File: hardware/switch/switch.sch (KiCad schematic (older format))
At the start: 27 parts, among them J1 Conn_01x07, J2 Conn_01x03, J3 Conn_01x05, J4 Conn_01x04, K1 G6SU-2, K2 G6SU-2, K3 G6SU-2, K4 G6SU-2, SW1 D2F-01, SW2 D2F-01, SW3 D2F-01, SW4 D2F-01, U1 NCV7718CDQR2G, U2 STM32F042F6Px, U3 NCV7428MW3

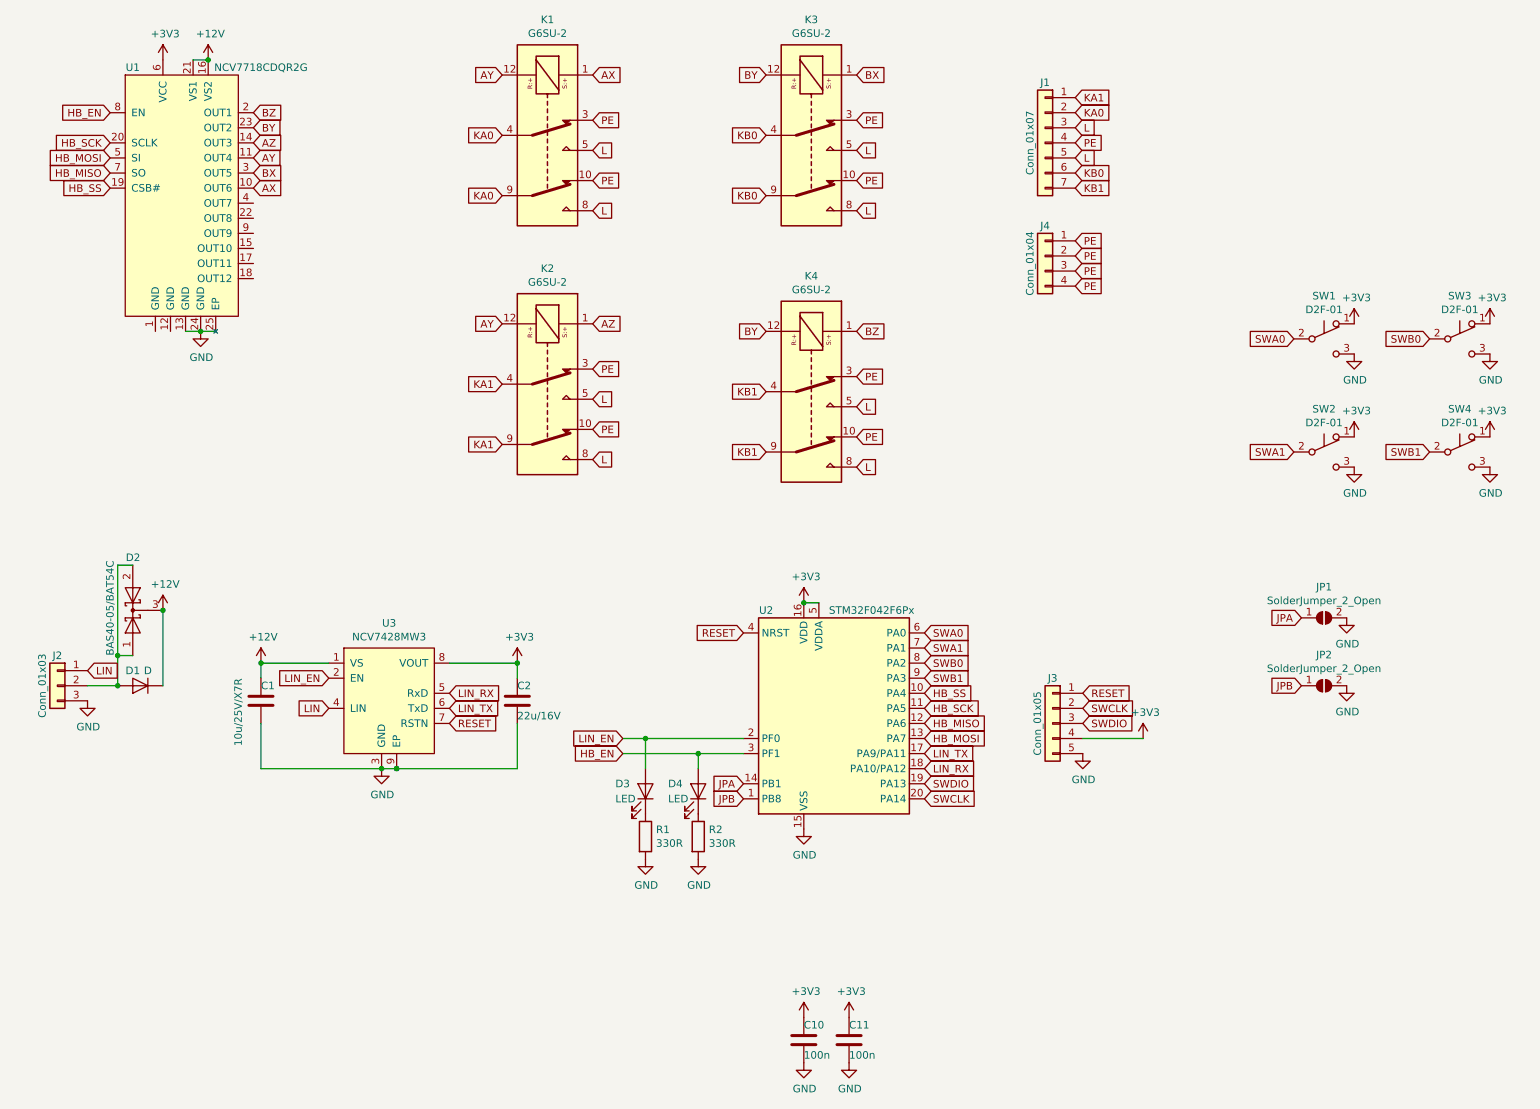
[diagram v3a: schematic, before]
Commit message: Add indicator LEDs to switch
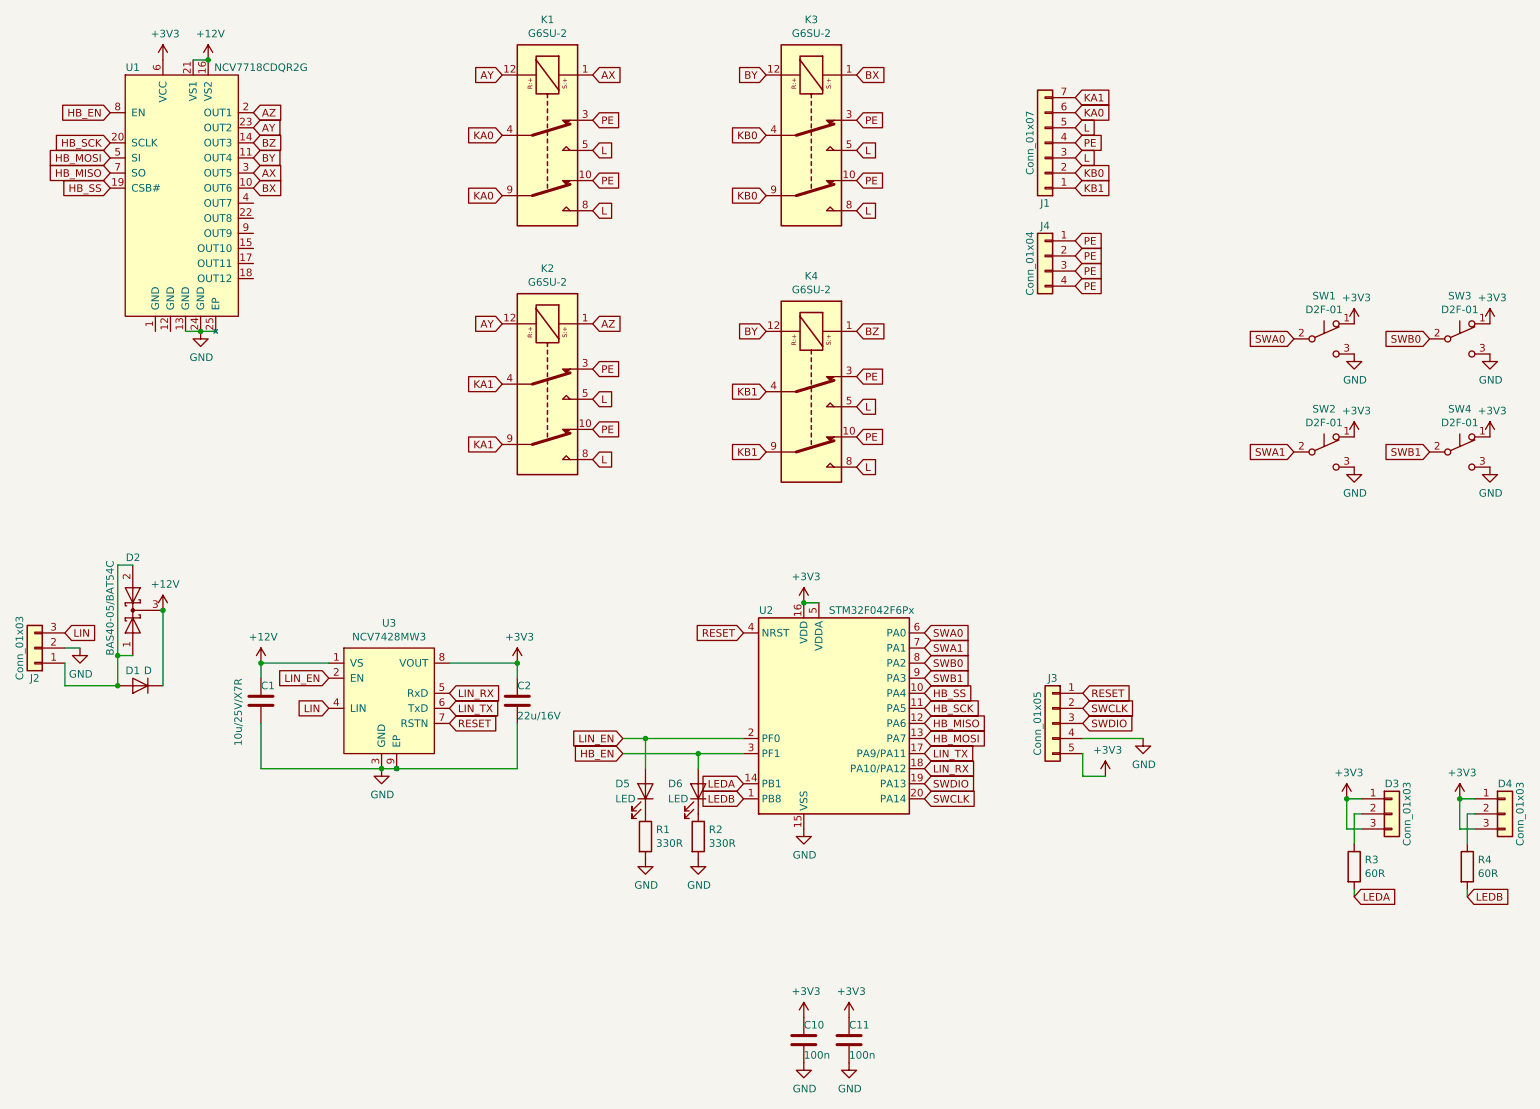
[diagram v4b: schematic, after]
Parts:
- removed JP1, JP2: SolderJumper_2_Open, RoomControl:Jumper2, symbol Jumper:SolderJumper_2_Open
- added D3, D4: Conn_01x03, RoomControl:DiodeHoles3, symbol Connector_Generic:Conn_01x03
- added R3, R4: 60R, Resistor_SMD:R_0603_1608Metric, symbol Device:R
- renumbered D3 to D5, D4 to D6, K3 to K1, K4 to K2, K1 to K3, K2 to K4, SW4 to SW1, SW3 to SW2, SW2 to SW3, SW1 to SW4
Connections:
- net +3V3: now also J3.5 (Pin_5), D3.1 (Pin_1), D3.3 (Pin_3), D4.1 (Pin_1), D4.3 (Pin_3); no longer J3.4 (Pin_4)
- net AX: now also K1.1, U1.3 (OUT5); no longer K3.1, U1.10 (OUT6)
- net AY: now also K1.12, K2.12, U1.23 (OUT2); no longer K3.12, K4.12, U1.11 (OUT4)
- net AZ: now also K2.1, U1.2 (OUT1); no longer K4.1, U1.14 (OUT3)
- net BX: now also K3.1, U1.10 (OUT6); no longer K1.1, U1.3 (OUT5)
- net BY: now also K3.12, K4.12, U1.11 (OUT4); no longer K1.12, K2.12, U1.23 (OUT2)
- net BZ: now also K4.1, U1.14 (OUT3); no longer K2.1, U1.2 (OUT1)
- net GND: now also J2.2 (Pin_2), J3.4 (Pin_4); no longer J2.3 (Pin_3), J3.5 (Pin_5)
- net KA0: now also J1.6 (Pin_6), K1.4, K1.9; no longer J1.2 (Pin_2), K3.4, K3.9
- net KA1: now also J1.7 (Pin_7), K2.4, K2.9; no longer J1.1 (Pin_1), K4.4, K4.9
- net KB0: now also J1.2 (Pin_2), K3.4, K3.9; no longer J1.6 (Pin_6), K1.4, K1.9
- net KB1: now also J1.1 (Pin_1), K4.4, K4.9; no longer J1.7 (Pin_7), K2.4, K2.9
- net LIN: now also J2.3 (Pin_3); no longer J2.1 (Pin_1)
- net SWA0: now also SW1.2 (B); no longer SW4.2 (B)
- net SWA1: now also SW2.2 (B); no longer SW3.2 (B)
- net SWB0: now also SW3.2 (B); no longer SW2.2 (B)
- net SWB1: now also SW4.2 (B); no longer SW1.2 (B)
- net at D1.2 (A), D2.1 (A), D2.2 (A): now also J2.1 (Pin_1); no longer J2.2 (Pin_2)
- net JPA renamed LEDA
- net LEDA: now also R3.2
- net JPB renamed LEDB
- net LEDB: now also R4.2
- new net: D3.2 (Pin_2), R3.1
- new net: D4.2 (Pin_2), R4.1
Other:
- moved on the sheet: J2, K1, K2, K3, K4, SW1, SW2, SW3, SW4
